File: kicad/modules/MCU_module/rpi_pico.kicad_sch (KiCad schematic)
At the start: 3 parts, among them SW1 Reset, U1 Pico

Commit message: Connector for bigger current, control module 2
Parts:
- D1: Mouser number (none) -> 78-VSKY02300603-G408
- SW1: Mouser number (none) -> 179-TS0925WT160SMTTR
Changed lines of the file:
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@@
 			)
 		)
-		(property "Description" ""
+		(property "Description" "RPI Pico 2"
+			(at 95.25 62.23 0)
+			(effects
+				(font
+					(size 1.27 1.27)
+				)
+				(hide yes)
+			)
+		)
+		(property "Manufacturer Part Number" ""
+			(at 95.25 62.23 0)
+			(effects
+				(font
+					(size 1.27 1.27)
+				)
+				(hide yes)
+			)
+		)
+		(property "Mouser number" ""
 			(at 95.25 62.23 0)
 			(effects
@@
 			)
 		)
-		(property "Description" "179-TS0925WT160SMTTR"
+		(property "Description" ""
+			(at 135.89 63.5 0)
+			(effects
+				(font
+					(size 1.27 1.27)
+				)
+				(hide yes)
+			)
+		)
+		(property "Manufacturer Part Number" ""
+			(at 135.89 63.5 0)
+			(effects
+				(font
+					(size 1.27 1.27)
+				)
+				(hide yes)
+			)
+		)
+		(property "Mouser number" "179-TS0925WT160SMTTR"
 			(at 135.89 63.5 0)
 			(effects
@@
 			)
 		)
-		(property "Description" "78-VSKY02300603-G408"
+		(property "Description" ""
 			(at 123.19 40.64 0)
 			(effects
+				(font
+					(size 1.27 1.27)
+				)
+				(hide yes)
+			)
+		)
+		(property "Manufacturer Part Number" ""
+			(at 123.19 40.64 0)
+			(effects
+				(font
+					(size 1.27 1.27)
+				)
+				(hide yes)
+			)
+		)
+		(property "Mouser number" "78-VSKY02300603-G408"
+			(at 123.19 40.64 0)
+			(effects

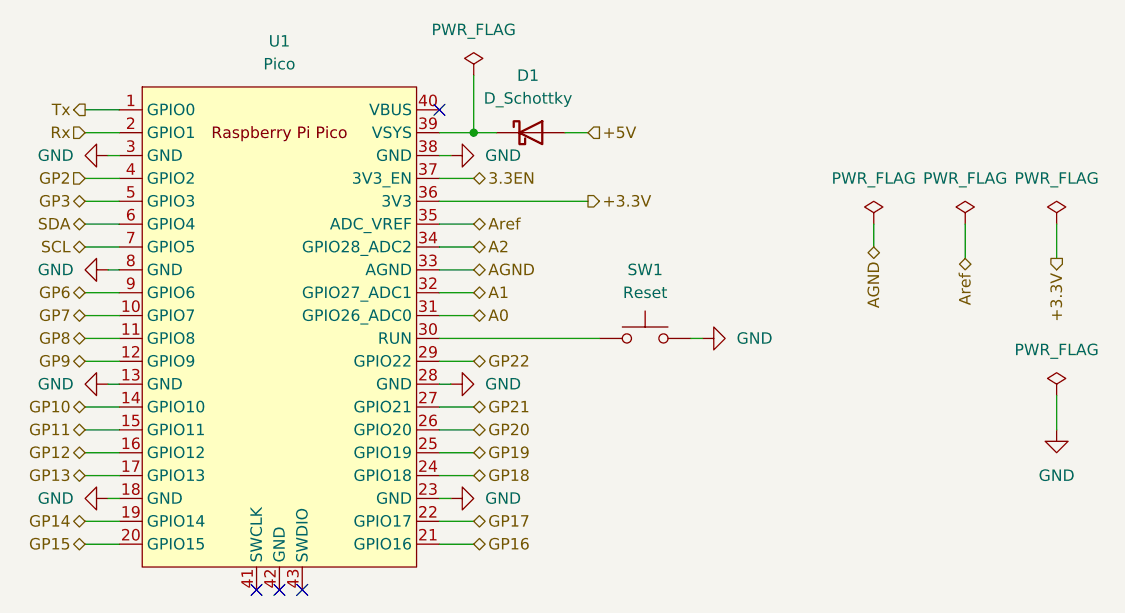
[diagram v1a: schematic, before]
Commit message: Add part numbers
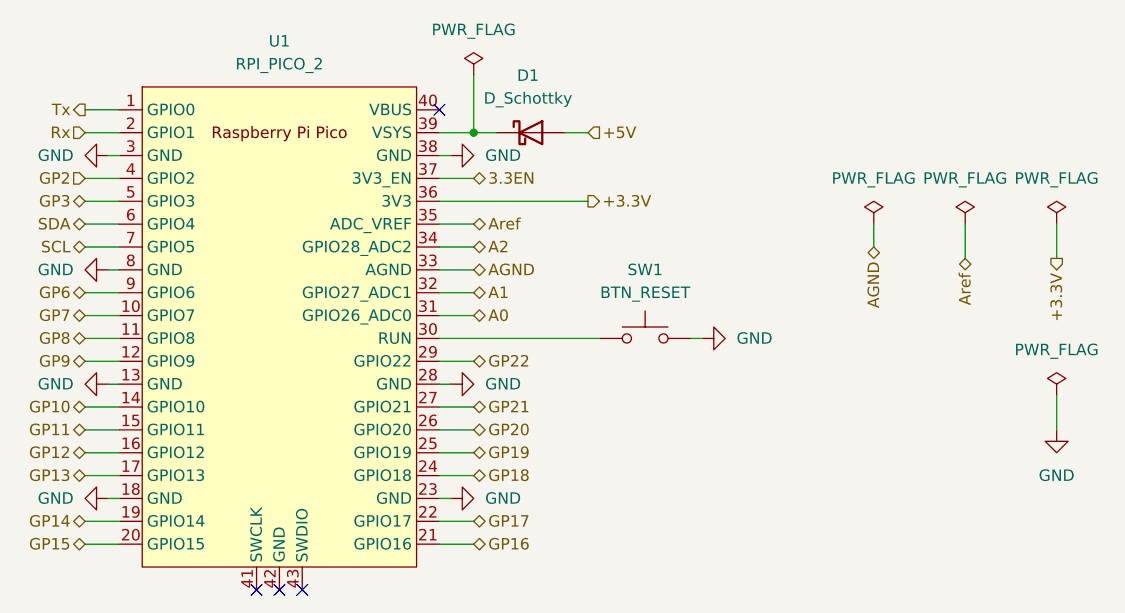
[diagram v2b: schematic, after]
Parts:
- D1: Manufacturer Part Number (none) -> VSKY02300603-G4-08
- SW1: value Reset -> BTN_RESET; Manufacturer Part Number (none) -> TS09-63-25-WT-160-SMT-TR
- U1: value Pico -> RPI_PICO_2; Manufacturer Part Number (none) -> SC1631; Mouser number (none) -> 358-SC1631
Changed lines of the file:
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@@
 			)
 		)
-		(property "Value" "Pico"
+		(property "Value" "RPI_PICO_2"
 			(at 95.25 33.02 0)
 			(effects
@@
 			)
 		)
-		(property "Description" "RPI Pico 2"
+		(property "Description" "CUSTOM"
 			(at 95.25 62.23 0)
 			(effects
@@
 			)
 		)
-		(property "Manufacturer Part Number" ""
+		(property "Manufacturer Part Number" "SC1631"
 			(at 95.25 62.23 0)
 			(effects
@@
 			)
 		)
-		(property "Mouser number" ""
+		(property "Mouser number" "358-SC1631"
 			(at 95.25 62.23 0)
 			(effects
@@
 			)
 		)
-		(property "Value" "Reset"
+		(property "Value" "BTN_RESET"
 			(at 135.89 58.42 0)
 			(effects
@@
 			)
 		)
-		(property "Description" ""
+		(property "Description" "CUSTOM"
 			(at 135.89 63.5 0)
 			(effects
@@
 			)
 		)
-		(property "Manufacturer Part Number" ""
+		(property "Manufacturer Part Number" "TS09-63-25-WT-160-SMT-TR "
 			(at 135.89 63.5 0)
 			(effects
@@
 			)
 		)
-		(property "Description" ""
+		(property "Description" "CUSTOM"
 			(at 123.19 40.64 0)
 			(effects
@@
 			)
 		)
-		(property "Manufacturer Part Number" ""
+		(property "Manufacturer Part Number" "VSKY02300603-G4-08"
 			(at 123.19 40.64 0)
 			(effects

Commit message: LED footprint update
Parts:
- D1: footprint Diode_SMD:D_0603_1608Metric_Pad1.05x0.95mm_HandSolder -> Diode_SMD:D_0805_2012Metric_Pad1.15x1.40mm_HandSolder; Manufacturer Part Number VSKY02300603-G4-08 -> SD0805S020S0R5; Mouser number 78-VSKY02300603-G408 -> 581-SD0805S020S0R5
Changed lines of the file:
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@@
 			)
 		)
-		(property "Footprint" "Diode_SMD:D_0603_1608Metric_Pad1.05x0.95mm_HandSolder"
+		(property "Footprint" "Diode_SMD:D_0805_2012Metric_Pad1.15x1.40mm_HandSolder"
 			(at 123.19 40.64 0)
 			(effects
@@
 			)
 		)
-		(property "Manufacturer Part Number" "VSKY02300603-G4-08"
+		(property "Manufacturer Part Number" "SD0805S020S0R5"
 			(at 123.19 40.64 0)
 			(effects
@@
 			)
 		)
-		(property "Mouser number" "78-VSKY02300603-G408"
+		(property "Mouser number" "581-SD0805S020S0R5"
 			(at 123.19 40.64 0)
 			(effects
